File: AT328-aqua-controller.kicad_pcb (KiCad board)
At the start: 2 copper layers, 76.6 x 76 mm, 46 parts, among them Q1 IRL520N, Q2 IRL520N, Q3 IRL520N, Q4 IRL520N, Q5 BC547, U1 ATmega328P-PU, U2 LM7805_TO220, Y1 16MHz

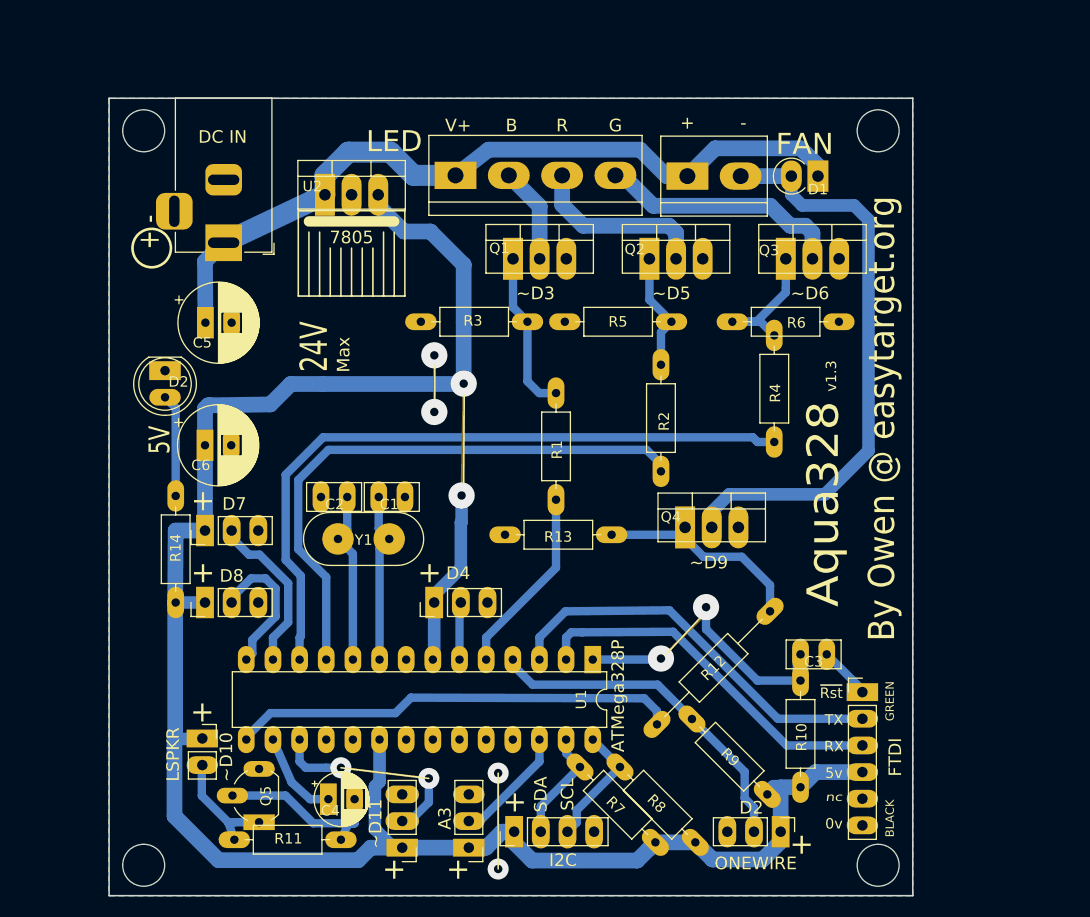
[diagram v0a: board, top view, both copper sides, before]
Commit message: Start on V2 PCB, relocated and duplicated connectors, reset jumper.
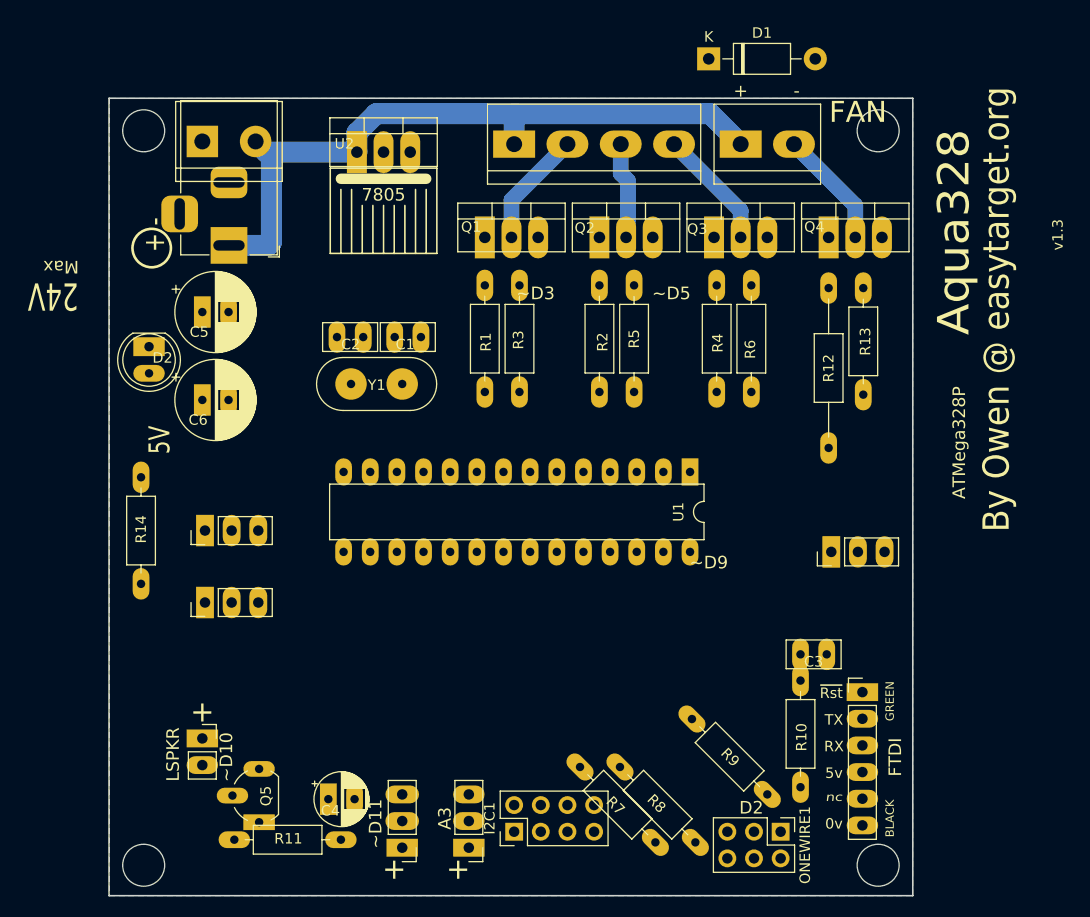
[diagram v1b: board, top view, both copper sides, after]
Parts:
- added JDC_IN2: 12/24v, TerminalBlock:TerminalBlock_bornier-2_P5.08mm, F.Cu at (40.7, 31.6)
- D1: footprint Diode_THT:D_DO-41_SOD81_P2.54mm_Vertical_KathodeUp -> Diode_THT:D_DO-41_SOD81_P10.16mm_Horizontal
- I2C1: footprint Connector_PinHeader_2.54mm:PinHeader_1x04_P2.54mm_Vertical -> Connector_PinHeader_2.54mm:PinHeader_2x04_P2.54mm_Vertical
- ONEWIRE1: footprint Connector_PinHeader_2.54mm:PinHeader_1x03_P2.54mm_Vertical -> Connector_PinHeader_2.54mm:PinHeader_2x03_P2.54mm_Vertical
- moved BUTTON1 38.2 mm to (100.6, 70.7)
- moved R13 33.6 mm to (103.7, 45.6), turned to 270 degrees
- moved R12 31.3 mm to (100.4, 45.6), turned to 270 degrees
- moved Q4 30.8 mm to (100.4, 40.8)
- moved U1 20.1 mm to (87.2, 63.1)
- moved C1 15.3 mm to (61.5, 50.3)
- moved C2 15.3 mm to (53.5, 50.3)
- moved D1 15.3 mm to (89.0, 23.7), turned to 0 degrees
- moved Y1 14.8 mm to (59.7, 54.7)
- moved R1 12.3 mm to (67.6, 45.3)
- moved R2 9.57 mm to (78.5, 45.3)
- moved R4 7.27 mm to (89.7, 45.3)
- moved Q3 7.14 mm to (89.5, 40.8)
- moved ABRG_LED1 6.33 mm to (70.4, 31.9)
- moved FAN1 5.92 mm to (92.0, 31.9)
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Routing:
- net +5V: track 213.9 -> 0.00 mm, vias 2 -> 0
- net LED-G: track 66.5 -> 0.00 mm
- net LED-R: track 55.2 -> 0.00 mm
- net Net-(D1-Pad2): track 55.5 -> 11.3 mm
- net FAN: track 43.7 -> 0.00 mm
- net TX: track 38.2 -> 0.00 mm
- net RX: track 35.0 -> 0.00 mm
- net 1WIRE: track 33.6 -> 0.00 mm
- net Net-(C3-Pad2): track 29.7 -> 0.00 mm, vias 2 -> 0
- net Net-(Q4-Pad1): track 20.8 -> 0.00 mm
- net AUX1: track 20.3 -> 0.00 mm, vias 2 -> 0
- net LED-B: track 18.0 -> 0.00 mm
- net Net-(C4-Pad2): track 17.3 -> 0.00 mm
- net Net-(C2-Pad2): track 16.5 -> 0.00 mm
- net Net-(C1-Pad2): track 16.3 -> 0.00 mm
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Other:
- board text removed: "~~D6"
